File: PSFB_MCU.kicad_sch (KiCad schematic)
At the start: 84 parts, among them Q1 WMM043N10HGD, Q2 WMM043N10HGD, Q3 WMM043N10HGD, Q4 WMM043N10HGD, U3 AMS1117-3.3, U4 LM5176PWP, U5 AMS1117-5.0

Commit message: VER1.0: добавил 4 канала управления драйверами
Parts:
- removed C20: 1n, Capacitor_SMD:C_0805_2012Metric_Pad1.18x1.45mm_HandSolder, symbol Device:C_Small
- added C18: 2.2u, Capacitor_SMD:C_1210_3225Metric_Pad1.33x2.70mm_HandSolder, symbol Device:C_Small
- added D11: D_TVS_Small, Diode_SMD:D_SMB_Handsoldering, symbol Device:D_TVS_Small
- added D14, D15: (no value), LED_SMD:LED_0805_2012Metric, symbol Device:LED_Small
- added J1: Power_IN, Connector_Molex:Molex_Mini-Fit_Jr_5566-04A_2x02_P4.20mm_Vertical, symbol Connector_Generic:Conn_02x02_Top_Bottom
- added L2: 10u, Inductor_SMD:L_Panasonic_PCC-M1040ML, symbol Device:L
- added R25, R26: 3k, Resistor_SMD:R_0805_2012Metric_Pad1.20x1.40mm_HandSolder, symbol Device:R_Small
- C1: renamed from C22; footprint Capacitor_SMD:C_0603_1608Metric_Pad1.08x0.95mm_HandSolder -> Capacitor_SMD:C_0805_2012Metric_Pad1.18x1.45mm_HandSolder
- C10: renamed from C6; footprint Capacitor_SMD:C_0603_1608Metric_Pad1.08x0.95mm_HandSolder -> Capacitor_SMD:C_0805_2012Metric_Pad1.18x1.45mm_HandSolder
- C11: renamed from C7; footprint Capacitor_SMD:C_0603_1608Metric_Pad1.08x0.95mm_HandSolder -> Capacitor_SMD:C_0805_2012Metric_Pad1.18x1.45mm_HandSolder
- C12: renamed from C8; footprint Capacitor_SMD:C_0603_1608Metric_Pad1.08x0.95mm_HandSolder -> Capacitor_SMD:C_0805_2012Metric_Pad1.18x1.45mm_HandSolder
- C13: renamed from C9; footprint Capacitor_SMD:C_0603_1608Metric_Pad1.08x0.95mm_HandSolder -> Capacitor_SMD:C_0805_2012Metric_Pad1.18x1.45mm_HandSolder
- C14: renamed from C10; footprint Capacitor_SMD:C_0603_1608Metric_Pad1.08x0.95mm_HandSolder -> Capacitor_SMD:C_0805_2012Metric_Pad1.18x1.45mm_HandSolder
- C2: renamed from C1; footprint Capacitor_SMD:C_0603_1608Metric_Pad1.08x0.95mm_HandSolder -> Capacitor_SMD:C_0805_2012Metric_Pad1.18x1.45mm_HandSolder
- C3: renamed from C2; footprint Capacitor_SMD:C_0603_1608Metric_Pad1.08x0.95mm_HandSolder -> Capacitor_SMD:C_0805_2012Metric_Pad1.18x1.45mm_HandSolder
- C4: renamed from C3; footprint Capacitor_SMD:C_0603_1608Metric_Pad1.08x0.95mm_HandSolder -> Capacitor_SMD:C_0805_2012Metric_Pad1.18x1.45mm_HandSolder
- C5: renamed from C4; footprint Capacitor_SMD:C_0603_1608Metric_Pad1.08x0.95mm_HandSolder -> Capacitor_SMD:C_0805_2012Metric_Pad1.18x1.45mm_HandSolder
- C9: renamed from C5; footprint Capacitor_SMD:C_0603_1608Metric_Pad1.08x0.95mm_HandSolder -> Capacitor_SMD:C_0805_2012Metric_Pad1.18x1.45mm_HandSolder
- renumbered C35 to C15, C11 to C16, C39 to C17, C34 to C19, C40 to C20, C45 to C21, C46 to C22, C38 to C23, C47 to C24, C49 to C25, C48 to C26, C23 to C27, C16 to C28, C17 to C29, C21 to C30, C18 to C31, C33 to C32, C36 to C33, C12 to C34, C37 to C35, C19 to C36, C13 to C6, C14 to C7, C15 to C8, D3 to D1, D5 to D10, D10 to D12, D11 to D13, D4 to D2, D1 to D3, D2 to D4, D6 to D5, D8 to D6, D12 to D7, D7 to D8, Q3 to Q2, Q2 to Q3, R20 to R10, R8 to R11, R14 to R12, R12 to R14, R22 to R15, R4 to R16, R23 to R17, R11 to R18, R17 to R19, R21 to R20, R6 to R21, R18 to R22, R10 to R23, R9 to R24, R5 to R3, R7 to R4, R3 to R5, R16 to R6, R15 to R7, R19 to R8, R24 to R9, U6 to U1, U1 to U2, U5 to U3, U3 to U4, U4 to U5
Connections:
- net PWM1_L_1 is gone; now on net TMR1_CH1N: U2.34 (PB13)
- net +24V: now also D15.2 (A)
- net GND_IN: now also R18.2, C18.1, D11.1 (A1), J1.3 (Pin_3), J1.4 (Pin_4), R25.2, R26.2; no longer R18.1
- net VIN: now also D14.2 (A), J1.1 (Pin_1), J1.2 (Pin_2), L2.1; no longer C19.1, C20.2, D7.2 (A), Q1.2 (D), R12.2, R22.2, R6.1
- net at U5.6 (RT/SYNC): now also R18.1; no longer R18.2
- net TMR1_CH1N: now reaches U2.23 (PA7)
- net PWM1_H_1 renamed TMR1_CH1
- net PWM1_H_2 renamed TMR8_CH1
- net PWM1_L_2 renamed TMR8_CH1N
- net PWM2_H_1 renamed TMR1_CH2
- net PWM2_H_2 renamed TMR8_CH2
- net PWM2_L_1 renamed TMR8_CH2N
- net PWM2_L_2 renamed TMR1_CH2N
- net PWM3_H_1: no longer names the net of U2.43 (PA10)
- net PWM3_H_2: no longer names the net of U2.39 (PC8)
- net PWM3_L_1: no longer names the net of U2.36 (PB15)
- net PWM3_L_2: no longer names the net of U2.27 (PB1)
- new net: D15.1 (K), R26.1
- new net: D14.1 (K), R25.1
- new net VIN_filtered: C18.2, C19.1, C20.2, D11.2 (A2), D7.2 (A), L2.2, Q1.2 (D), R12.2, R22.2, R6.1
- no-connect marks 11 -> 32
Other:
- added sheet PSFB_Control_1 (PSFB_Control.kicad_sch)
- added sheet PSFB_Control_2 (PSFB_Control.kicad_sch)
- added sheet PSFB_Control_3 (PSFB_Control.kicad_sch)
- added sheet PSFB_Control_4 (PSFB_Control.kicad_sch)
- moved on the sheet: R16, R18

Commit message: VER1.0: добавил схему с измерением напряжения и заменил LVDS трансиверы
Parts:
- removed C14: 2.2u, Capacitor_SMD:C_0805_2012Metric_Pad1.18x1.45mm_HandSolder, symbol Device:C_Small
- removed D3: (no value), Package_TO_SOT_SMD:SOT-23-3, symbol Power_Protection:ESDA5V3L
- removed R5: 1k, Resistor_SMD:R_0603_1608Metric_Pad0.98x0.95mm_HandSolder, symbol Device:R_Small
- removed U2: (no value), Package_QFP:LQFP-64_10x10mm_P0.5mm, symbol MCU_ST_STM32F4:STM32F405RGTx
- removed Y1: (no value), Crystal:Resonator_SMD_Murata_CSTxExxV-3Pin_3.0x1.1mm, symbol Device:Crystal_GND2
- added C12: 2.2u, Capacitor_SMD:C_0805_2012Metric_Pad1.18x1.45mm_HandSolder, symbol Device:C_Small
- added C2: 100n, Capacitor_SMD:C_0805_2012Metric_Pad1.18x1.45mm_HandSolder, symbol Device:C_Small
- added C3, C4: 12p, Capacitor_SMD:C_0805_2012Metric_Pad1.18x1.45mm_HandSolder, symbol Device:C_Small
- added D1: (no value), Diode_SMD:D_SOD-323_HandSoldering, symbol Device:D_Small
- added D5: (no value), LED_SMD:LED_0805_2012Metric, symbol Device:LED_Small
- added J1: (no value), Connector_PinHeader_2.54mm:PinHeader_1x04_P2.54mm_Vertical, symbol Connector_Generic:Conn_01x04
- added R3, R4: 20, Resistor_SMD:R_0805_2012Metric_Pad1.20x1.40mm_HandSolder, symbol Device:R_Small
- added R7, R8: 1k, Resistor_SMD:R_0805_2012Metric_Pad1.20x1.40mm_HandSolder, symbol Device:R_Small
- added U2: (no value), Package_TO_SOT_SMD:SOT-23-6, symbol Power_Protection:USBLC6-2SC6
- added U3: (no value), Package_QFP:LQFP-64_10x10mm_P0.5mm, symbol MCU_ST_STM32F4:STM32F405RGTx
- added Y1: 16M, Crystal:Crystal_SMD_SeikoEpson_FA238-4Pin_3.2x2.5mm, symbol Device:Crystal_GND24
- C13: Description P/N (none) -> Capacitor SMD 50V
- D4: footprint LED_SMD:LED_0603_1608Metric_Pad1.05x0.95mm_HandSolder -> LED_SMD:LED_0805_2012Metric
- R1, R2: value 1k -> 10k; footprint Resistor_SMD:R_0603_1608Metric_Pad0.98x0.95mm_HandSolder -> Resistor_SMD:R_0805_2012Metric_Pad1.20x1.40mm_HandSolder; Description P/N (none) -> Resistor SMD
- renumbered C7 to C10, C8 to C11, C9 to C14, C10 to C15, C11 to C16, C12 to C17, C15 to C18, C16 to C19, C17 to C20, C18 to C21, C19 to C22, C20 to C23, C21 to C24, C22 to C25, C23 to C26, C24 to C27, C25 to C28, C26 to C29, C27 to C30, C28 to C31, C29 to C32, C30 to C33, C31 to C34, C32 to C35, C33 to C36, C34 to C37, C35 to C38, C36 to C39, C2 to C5, C3 to C6, C4 to C7, C5 to C8, C6 to C9, D9 to D10, D10 to D11, D11 to D12, D12 to D13, D13 to D14, D14 to D15, D15 to D16, D1 to D2, D2 to D3, D5 to D6, D6 to D7, D7 to D8, D8 to D9, J1 to J2, R7 to R10, R8 to R11, R9 to R12, R10 to R13, R11 to R14, R12 to R15, R13 to R16, R14 to R17, R15 to R18, R16 to R19, R17 to R20, R18 to R21, R19 to R22, R20 to R23, R21 to R24, R22 to R25, R23 to R26, R24 to R27, R25 to R29, R26 to R30, R3 to R5, R4 to R6, R6 to R9, U3 to U4, U4 to U5, U5 to U6
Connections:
- net +3.3V: now also D1.1 (K), U2.5 (VBUS), U3.1 (VBAT), U3.13 (VDDA), U3.19 (VDD), U3.32 (VDD), U3.48 (VDD), U3.64 (VDD)
- net BOOT0: now also U3.60 (BOOT0)
- net GND: now also C12.2, C2.1, C3.1, C4.2, J1.1 (Pin_1), R7.2, R8.2, U2.2 (GND), U3.12 (VSSA), U3.18 (VSS), U3.63 (VSS), Y1.2, Y1.4
- net NRST: now also C2.2, U3.7 (NRST)
- net SWCLK: now also U2.1 (I/O1), U3.49 (PA14)
- net SWDIO: now also U2.3 (I/O2), U3.46 (PA13)
- net at D4.2 (A): now also U3.2 (PC13)
- net at C13.1: now also U3.47 (VCAP_2)
- net at D4.1 (K): now also R7.1
- new net: R4.1, U2.6 (I/O1)
- new net: J1.2 (Pin_2), R4.2
- new net: D5.2 (A), U3.3 (PC14)
- new net: C12.1, U3.31 (VCAP_1)
- new net: C3.2, U3.5 (PH0), Y1.3
- new net: C4.1, U3.6 (PH1), Y1.1
- new net: D1.2 (A), J1.4 (Pin_4)
- new net: D5.1 (K), R8.1
- new net: R3.1, U2.4 (I/O2)
- new net: J1.3 (Pin_3), R3.2
- new net CAN_RXD_MCU: U3.44 (PA11)
- new net CAN_TXD_MCU: U3.45 (PA12)
- new net ERROR_LvL1: U3.21 (PA5)
- new net ERROR_LvL2: U3.22 (PA6)
- new net ERROR_LvL3: U3.23 (PA7)
- new net GPIO1: U3.33 (PB12)
- new net GPIO2: U3.34 (PB13)
- new net GPIO3: U3.35 (PB14)
- new net GPIO4: U3.36 (PB15)
- new net GPIO5: U3.37 (PC6)
- new net GPIO6: U3.38 (PC7)
- new net GPIO7: U3.39 (PC8)
- new net GPIO8: U3.40 (PC9)
- new net RS_RXD_MCU: U3.43 (PA10)
- new net RS_TXD_MCU: U3.42 (PA9)
- new net Solenoid1_MCU: U3.50 (PA15)
- new net Solenoid2_MCU: U3.51 (PC10)
- new net Solenoid3_MCU: U3.52 (PC11)
- new net Solenoid4_MCU: U3.53 (PC12)
- no-connect marks 32 -> 10
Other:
- added sheet Connector_channel_1 (Connector.kicad_sch)
- added sheet Connector_channel_2 (Connector.kicad_sch)
- added sheet HVoltage_measure_1 (HV_measure.kicad_sch)
- added sheet LVoltage+measure (LV_measure.kicad_sch)
- sheet PSFB_Control_1 ports: added PWM_H_N, PWM_H_P, PWM_L_N, PWM_L_P; removed FAULT, ~{RST}
- sheet PSFB_Control_2 ports: added PWM_H_N, PWM_H_P, PWM_L_N, PWM_L_P; removed FAULT, ~{RST}
- sheet PSFB_Control_3 ports: added PWM_H_N, PWM_H_P, PWM_L_N, PWM_L_P; removed FAULT, ~{RST}
- sheet PSFB_Control_4 ports: added PWM_H_N, PWM_H_P, PWM_L_N, PWM_L_P; removed FAULT, ~{RST}
- note removed: "Питание МК"
- moved on the sheet: C14, C15, C16, C17, C18, C19, C20, C21, C22, C23, C24, C25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

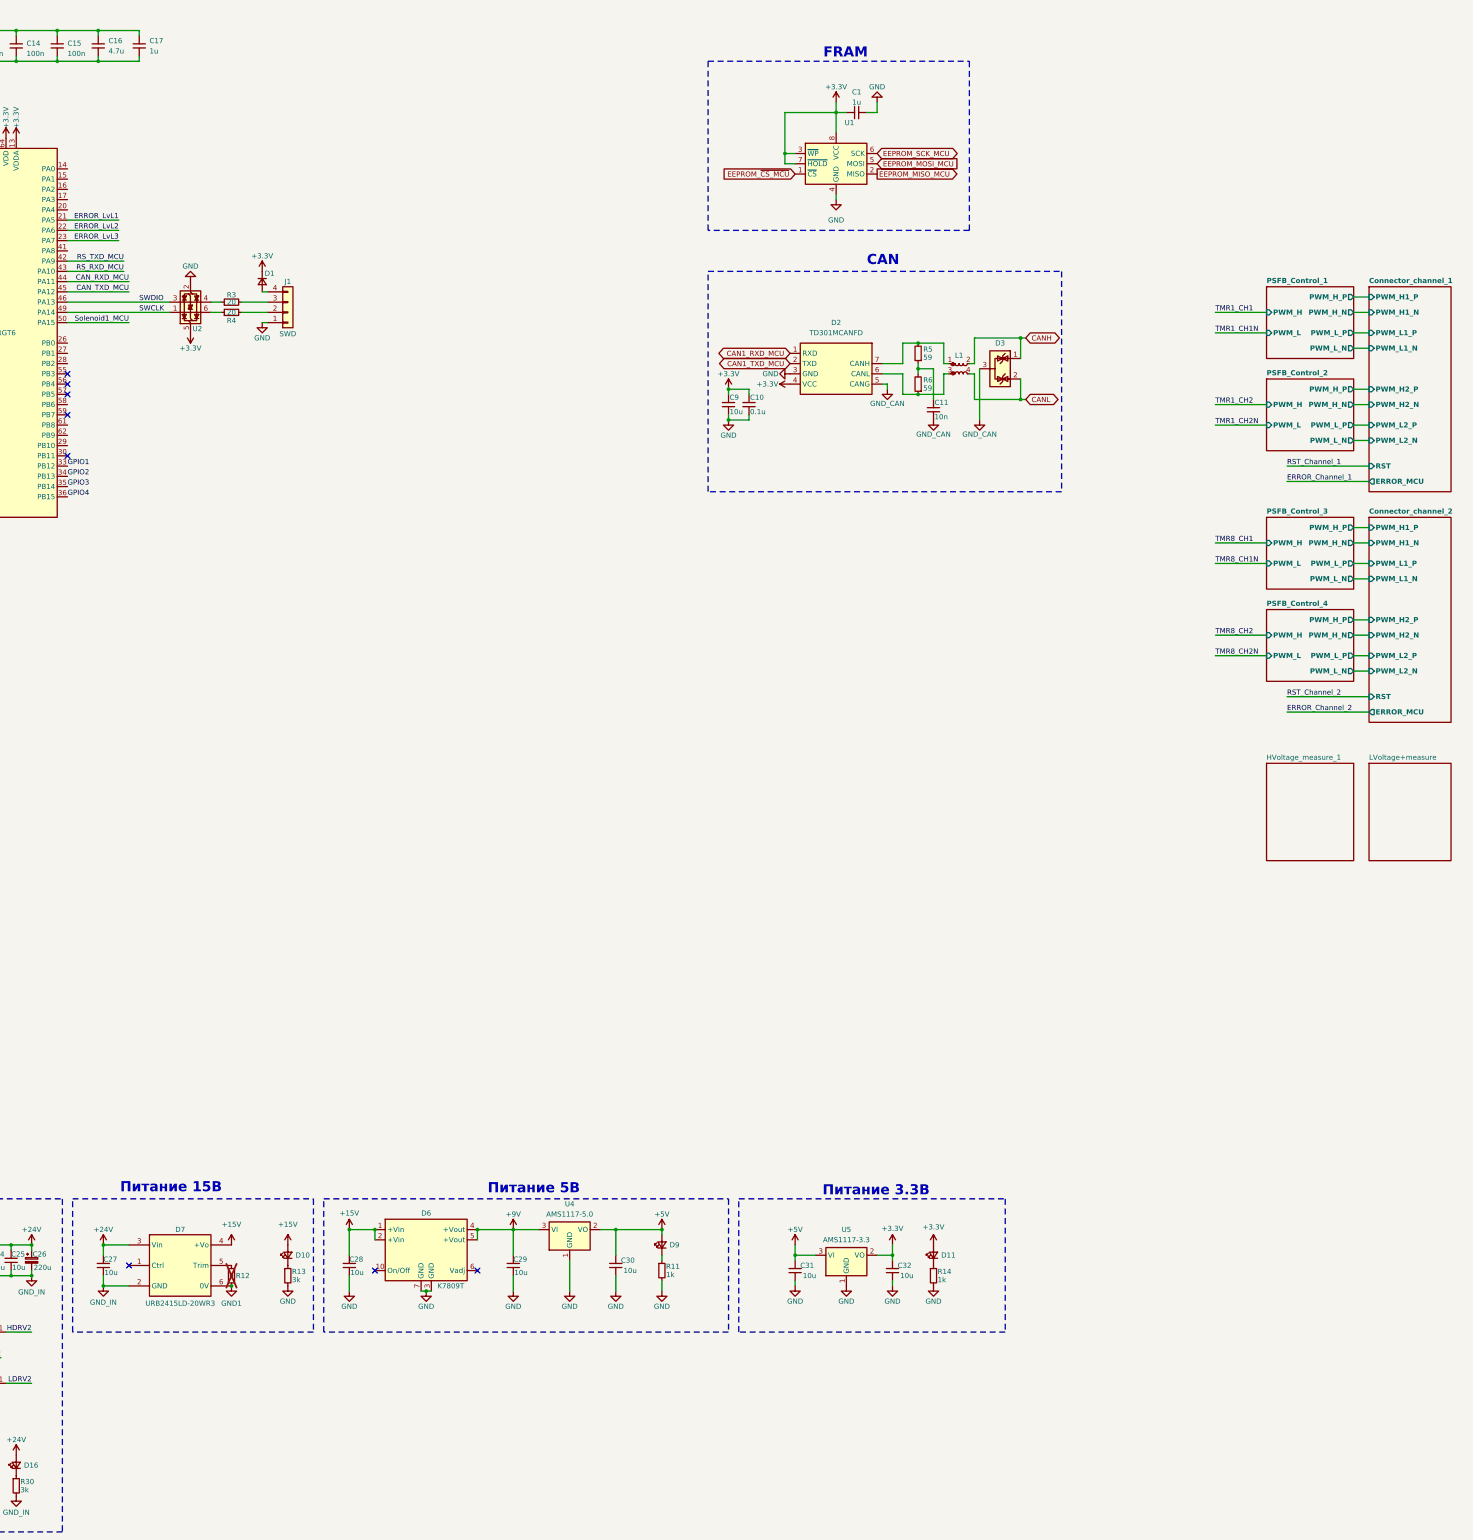
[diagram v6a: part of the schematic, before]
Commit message: VER1.0: добавил аппаратную защиту
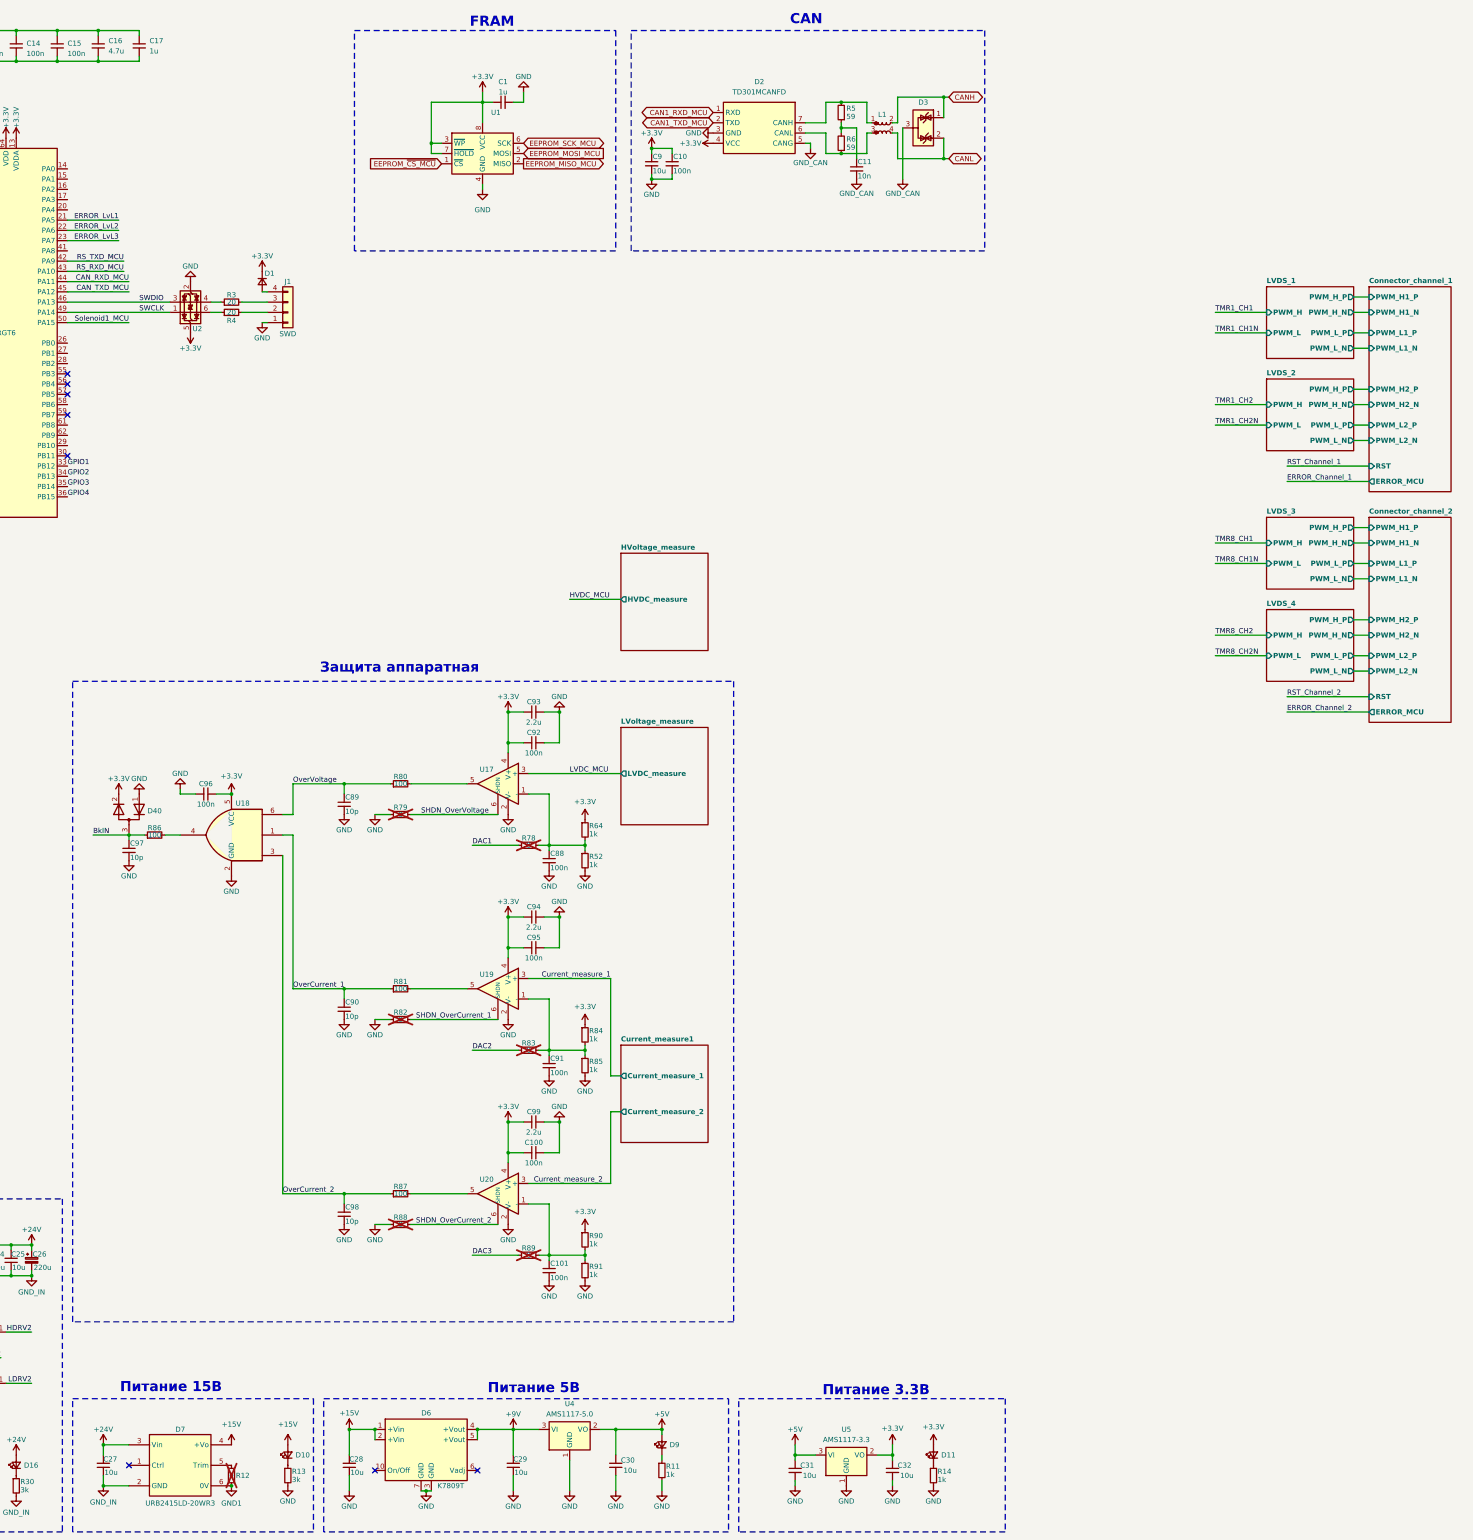
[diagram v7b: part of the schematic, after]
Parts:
- added C100, C101, C88, C91, C92, C95, C96: 100n, Capacitor_SMD:C_0805_2012Metric_Pad1.18x1.45mm_HandSolder, symbol Device:C_Small
- added C89, C90, C97, C98: 10p, Capacitor_SMD:C_0805_2012Metric_Pad1.18x1.45mm_HandSolder, symbol Device:C_Small
- added C93, C94, C99: 2.2u, Capacitor_SMD:C_0805_2012Metric_Pad1.18x1.45mm_HandSolder, symbol Device:C_Small
- added D40: (no value), Package_TO_SOT_SMD:SOT-23, symbol Device:D_Dual_Series_AKC_Parallel
- added R52, R64, R84, R85, R90, R91: 1k, Resistor_SMD:R_0805_2012Metric_Pad1.20x1.40mm_HandSolder, symbol Device:R_Small
- added R78, R79, R82, R83, R88, R89: 0, Resistor_SMD:R_0805_2012Metric_Pad1.20x1.40mm_HandSolder, symbol Device:R_Small
- added R80, R81, R86, R87: 100, Resistor_SMD:R_0805_2012Metric_Pad1.20x1.40mm_HandSolder, symbol Device:R_Small
- added U17, U19, U20: TLV3501AIDBV, Package_TO_SOT_SMD:SOT-23-6, symbol Comparator:TLV3501AIDBV
- added U18: 74LVC1G332, symbol 74xGxx:74LVC1G332
- C10: value 0.1u -> 100n
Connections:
- net +3.3V: now also C100.1, C92.1, C93.1, C94.1, C95.1, C96.2, C99.1, D40.2 (K), R64.1, R84.1, R90.1, U17.4 (V+), U18.5 (VCC), U19.4 (V+), U20.4 (V+)
- net GND: now also C100.2, C101.2, C88.2, C89.2, C90.2, C91.2, C92.2, C93.2, C94.2, C95.2, C96.1, C97.2, C98.2, C99.2, D40.1 (A), R52.2, R79.1, R82.1, R85.2, R88.1, R91.2, U17.2 (V-), U18.2 (GND), U19.2 (V-), U20.2 (V-)
- new net: C88.1, R52.1, R64.2, R78.2, U17.1 (-)
- new net: R81.2, U19.5
- new net: C91.1, R83.2, R84.2, R85.1, U19.1 (-)
- new net: C101.1, R89.2, R90.2, R91.1, U20.1 (-)
- new net: R80.2, U17.5
- new net: R86.2, U18.4
- new net: R87.2, U20.5
- new net BkIN: C97.1, D40.3 (common), R86.1
- new net Current_measure_1: U19.3 (+)
- new net Current_measure_2: U20.3 (+)
- new net DAC1: R78.1
- new net DAC2: R83.1
- new net DAC3: R89.1
- new net LVDC_MCU: U17.3 (+)
- new net OverCurrent_1: C90.1, R81.1, U18.1
- new net OverCurrent_2: C98.1, R87.1, U18.3
- new net OverVoltage: C89.1, R80.1, U18.6
- new net SHDN_OverCurrent_1: R82.2, U19.6 (SHDN)
- new net SHDN_OverCurrent_2: R88.2, U20.6 (SHDN)
- new net SHDN_OverVoltage: R79.2, U17.6 (SHDN)
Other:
- sheet HVoltage_measure_1 renamed HVoltage_measure
- sheet LVoltage+measure renamed LVoltage_measure
- sheet PSFB_Control_1 renamed LVDS_1
- sheet PSFB_Control_2 renamed LVDS_2
- sheet PSFB_Control_3 renamed LVDS_3
- sheet PSFB_Control_4 renamed LVDS_4
- added sheet Current_measure1 (Current_measure.kicad_sch)
- sheet HVoltage_measure ports: added HVDC_measure; removed none
- sheet LVoltage_measure ports: added LVDC_measure; removed none
- note added: "Защита аппаратная"
- moved on the sheet: C1, C10, C11, C27, C28, C29, C30, C31, C32, C9, D10, D11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
